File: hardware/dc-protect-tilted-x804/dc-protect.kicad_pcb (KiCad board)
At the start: 2 copper layers, 53.6 x 59.9 mm, 9 parts, among them P1 CON-SENSOR2-BLANK, U1 DC-Protect

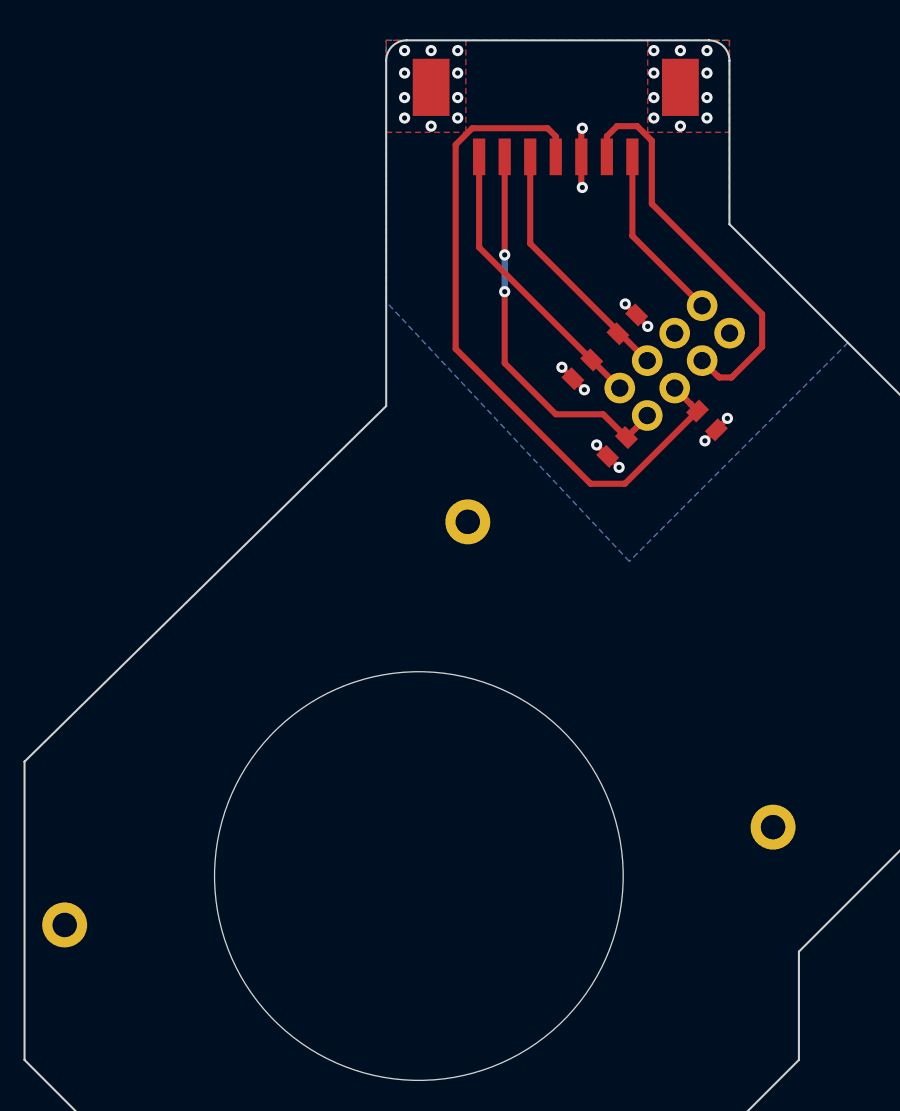
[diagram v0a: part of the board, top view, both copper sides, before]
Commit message: Hardware: dc-protect-tilted-x804 V1.4 Added 2 DNP-C footprints, Pin 7 disconnect, added fiducials
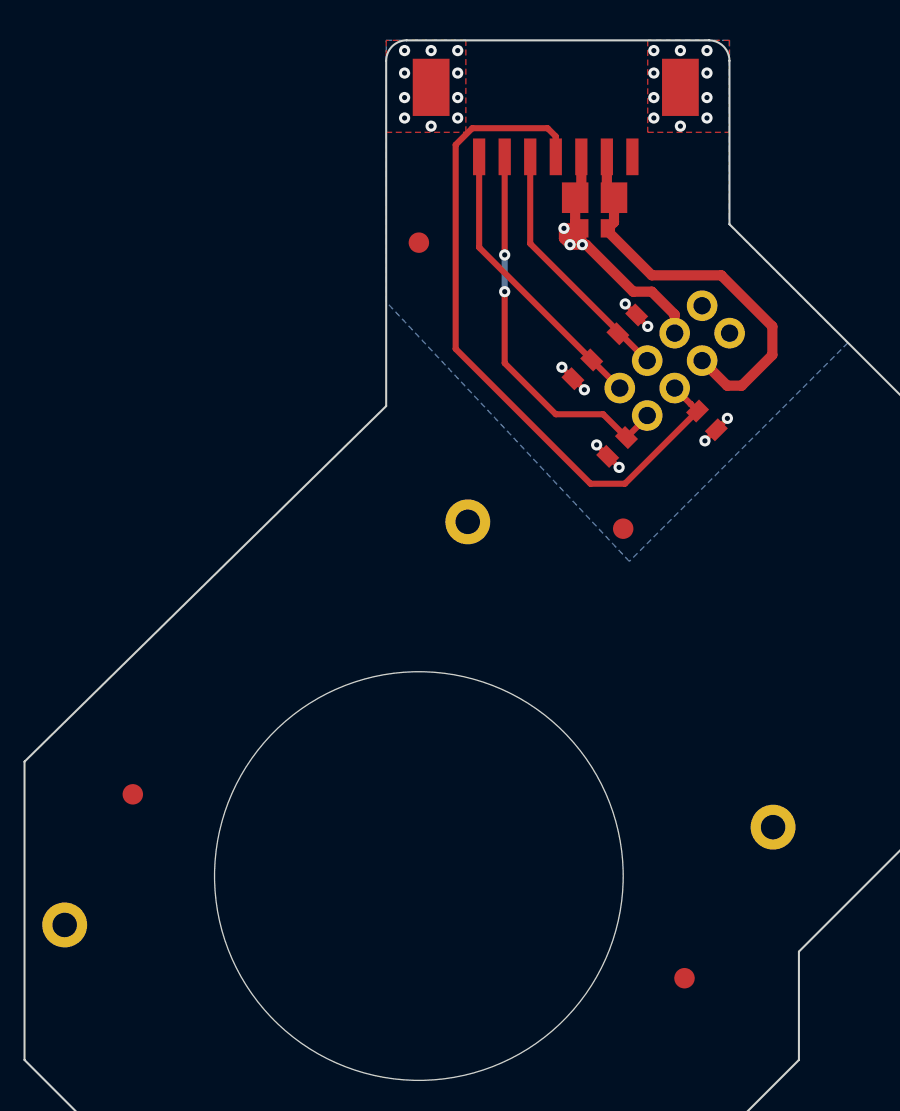
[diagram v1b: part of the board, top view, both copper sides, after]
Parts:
- added C5: DNP, kicad-libraries:C0805E, F.Cu at (204.9, 60.2)
- added C6: DNP, kicad-libraries:C0402E, F.Cu at (204.9, 61.7)
- added Fiducial_Mark: VAL**, kicad-libraries:Fiducial_Mark, F.Cu at (206.3, 76.4)
- added Fiducial_Mark: VAL**, kicad-libraries:Fiducial_Mark, F.Cu at (209.3, 98.4)
- added Fiducial_Mark: VAL**, kicad-libraries:Fiducial_Mark, F.Cu at (182.3, 89.4)
- added Fiducial_Mark: VAL**, kicad-libraries:Fiducial_Mark, F.Cu at (196.3, 62.4)
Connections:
- P1 pad 7: Net-(P1-Pad7) -> unconnected-(P1-Pad7)
- U1 pad 7: Net-(P1-Pad7) -> unconnected-(U1-Pad7)
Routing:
- net GND: track 9.21 -> 21.8 mm, vias 30 -> 31
- net Net-(P1-Pad7): track 8.70 -> 0.00 mm
- net Net-(C2-Pad1): track 19.7 -> 19.1 mm
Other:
- board text added: "DC-Protect 1.4"
- board text removed: "DC-Protect 1.3"

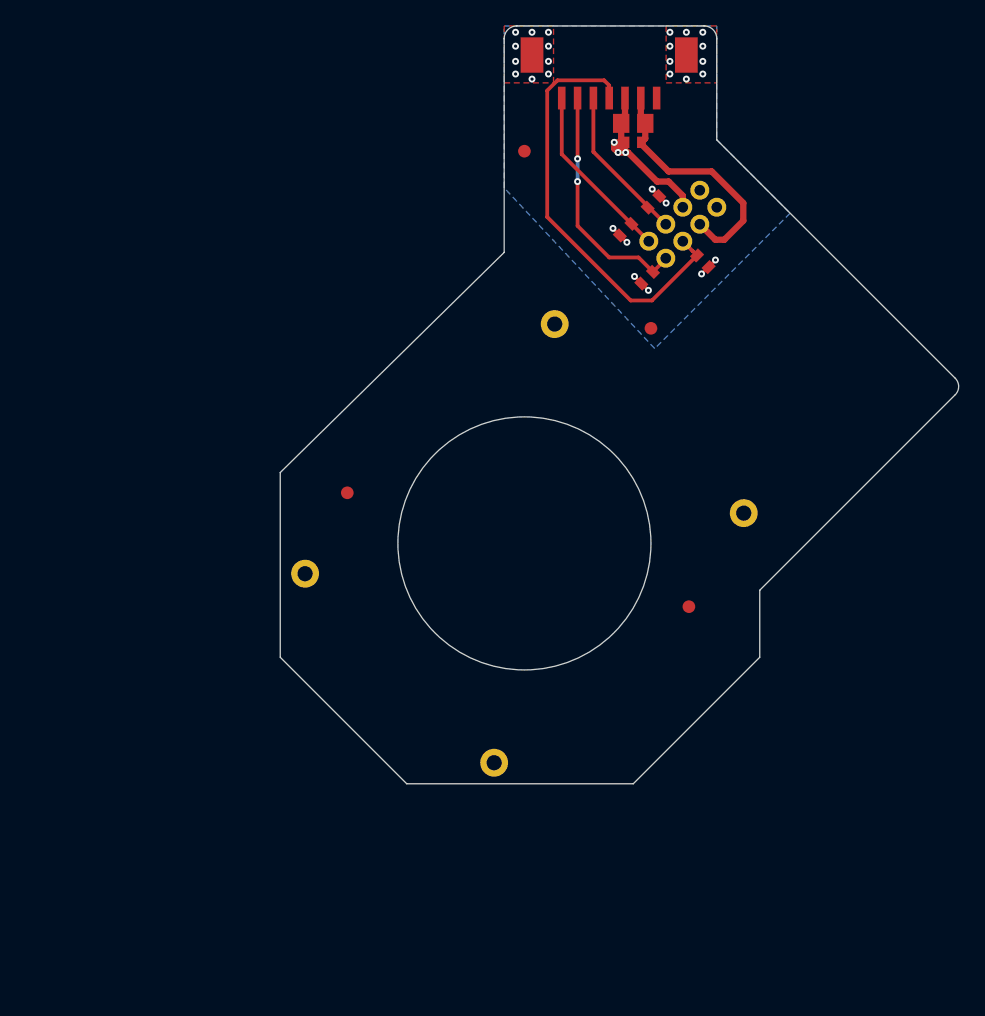
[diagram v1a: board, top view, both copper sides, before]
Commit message: fix dc protect outline, move to mm (54x60)
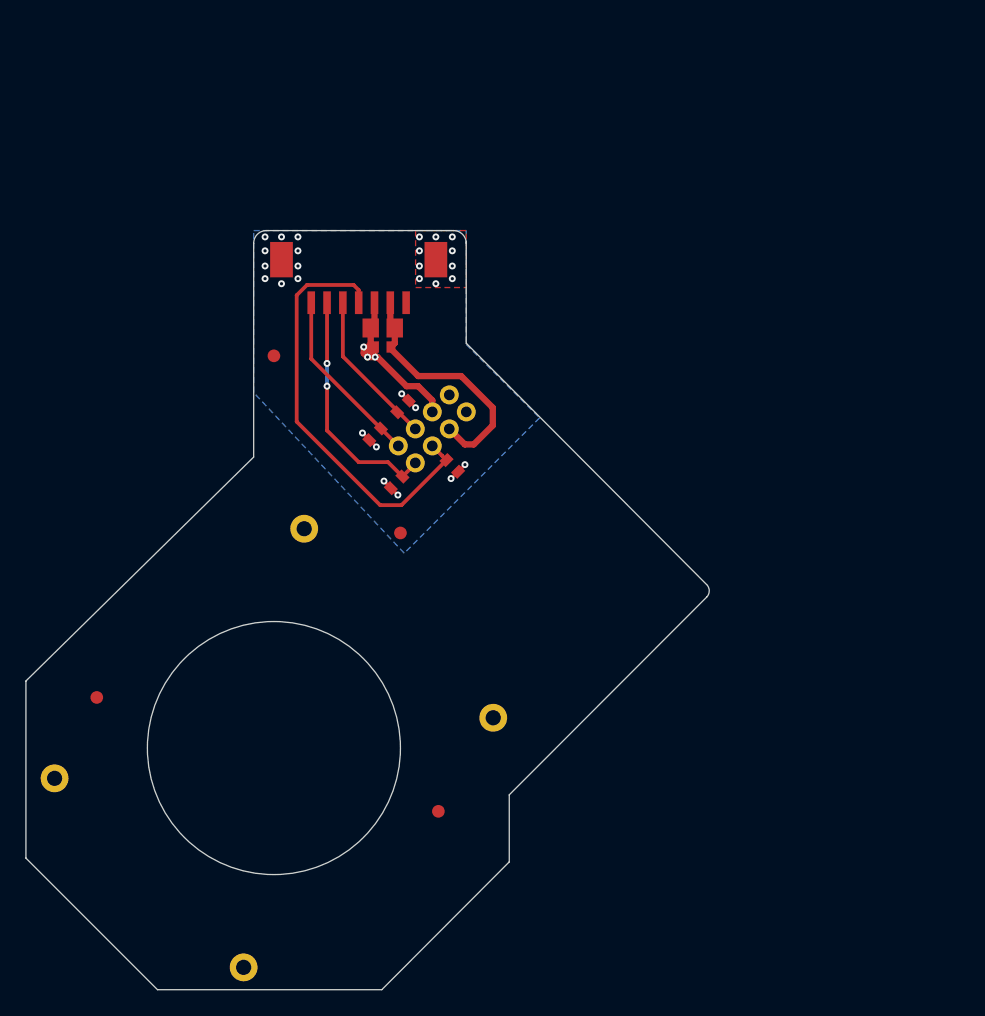
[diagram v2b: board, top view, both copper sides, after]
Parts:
- removed the Fiducial_Mark at (206.3, 76.4)
- removed the Fiducial_Mark at (209.3, 98.4)
- removed the Fiducial_Mark at (182.3, 89.4)
- removed the Fiducial_Mark at (196.3, 62.4)
- added Fiducial_Mark: VAL**, kicad-libraries:Fiducial_Mark, F.Cu at (186.5, 92.6)
- added Fiducial_Mark: VAL**, kicad-libraries:Fiducial_Mark, F.Cu at (176.5, 78.6)
- added Fiducial_Mark: VAL**, kicad-libraries:Fiducial_Mark, F.Cu at (189.5, 114.6)
- added Fiducial_Mark: VAL**, kicad-libraries:Fiducial_Mark, F.Cu at (162.5, 105.6)
- moved C1 25.6 mm to (184.5, 84.8)
- moved C4 25.6 mm to (190.6, 87.3)
- moved G*** 25.6 mm to (181.6, 121.3)
- moved P1 25.6 mm to (183.2, 69.6)
- moved C2 25.6 mm to (186.2, 88.6)
- moved C3 25.6 mm to (186.7, 82.6)
- moved C5 25.6 mm to (185.1, 76.4)
- moved C6 25.6 mm to (185.1, 77.9)
- moved U1 25.6 mm to (176.5, 109.6)
- moved VAL 25.6 mm to (169.0, 122.6)
- moved G*** 25.6 mm to (193.8, 97.2)
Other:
- board size 53.6 x 59.9 mm -> 54 x 60 mm
- board text added: "Copyright Tinkerforge GmbH 2023. This documentation describes Open Hardware and is licensed under the CERN OHL v. 1.1. You may redistribute and modify this documentation under the terms of the CERN OHL v.1.1. (http://ohwr.org/cernohl). This documentation is distributed WITHOUT ANY EXPRESS OR IMPLIED WARRANTY, INCLUDING OF MERCHANTABILITY, SATISFACTORY QUALITY AND FITNESS FOR A PARTICULAR PURPOSE.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"
- board text removed: "Copyright Tinkerforge GmbH 2021. This documentation describes Open Hardware and is licensed under the CERN OHL v. 1.1. You may redistribute and modify this documentation under the terms of the CERN OHL v.1.1. (http://ohwr.org/cernohl). This documentation is distributed WITHOUT ANY EXPRESS OR IMPLIED WARRANTY, INCLUDING OF MERCHANTABILITY, SATISFACTORY QUALITY AND FITNESS FOR A PARTICULAR PURPOSE.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"
